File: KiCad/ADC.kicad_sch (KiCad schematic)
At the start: 35 parts, among them U10 MCP3564-EST, U11 REF4132B25DBVR, U9 OPA2342UA

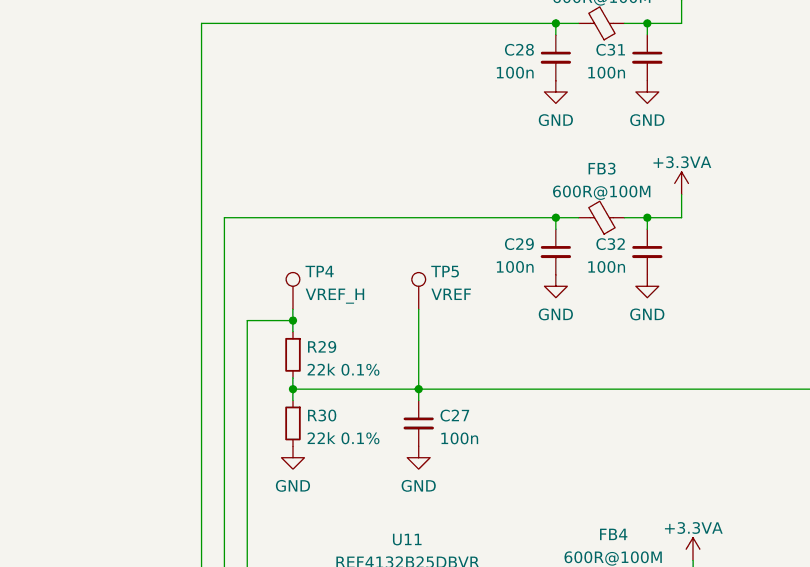
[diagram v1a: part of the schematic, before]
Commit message: Update KiCad project to newest version
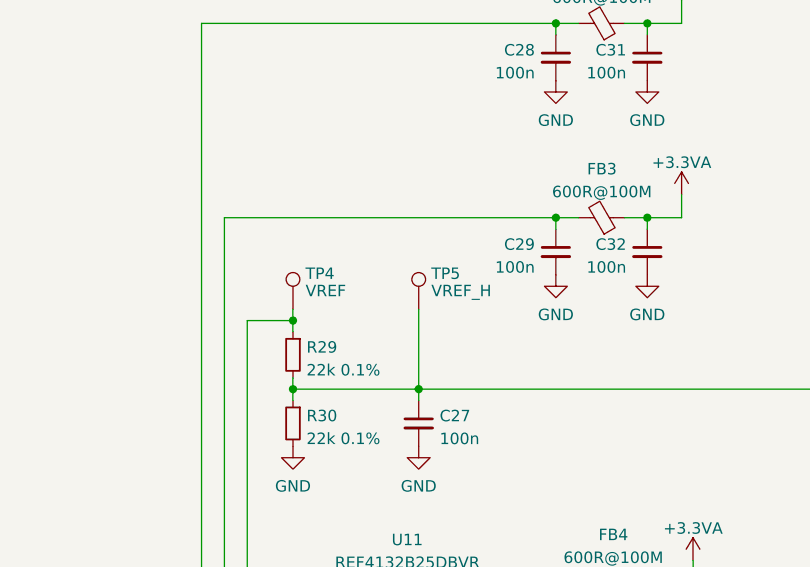
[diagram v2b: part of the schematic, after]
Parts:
- TP4: value VREF_H -> VREF
- TP5: value VREF -> VREF_H
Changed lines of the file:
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@@
   (symbol (lib_id "Connector:TestPoint") (at 156.21 52.07 0) (unit 1)
     (in_bom yes) (on_board yes) (dnp no) (fields_autoplaced)
-    (property "Reference" "TP4" (at 157.607 47.9333 0)
-      (effects (font (size 1.27 1.27)) (justify left))
-    )
-    (property "Value" "VREF_H" (at 157.607 50.4702 0)
+    (property "Reference" "TP4" (at 157.607 48.1243 0)
+      (effects (font (size 1.27 1.27)) (justify left))
+    )
+    (property "Value" "VREF" (at 157.607 50.0453 0)
       (effects (font (size 1.27 1.27)) (justify left))
     )
@@
   (symbol (lib_id "Connector:TestPoint") (at 170.18 52.07 0) (unit 1)
     (in_bom yes) (on_board yes) (dnp no) (fields_autoplaced)
-    (property "Reference" "TP5" (at 171.577 47.9333 0)
-      (effects (font (size 1.27 1.27)) (justify left))
-    )
-    (property "Value" "VREF" (at 171.577 50.4702 0)
-      (effects (font (size 1.27 1.27)) (justify left))
-    )
+    (property "Reference" "TP5" (at 171.577 48.1243 0)
+      (effects (font (size 1.27 1.27)) (justify left))
+    )
+    (property "Value" "VREF_H" (at 171.577 50.0453 0)
+      (effects (font (size 1.27 1.27)) (justify left))
+    )
